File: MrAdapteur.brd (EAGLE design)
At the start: 91 x 41.3 mm, 12 parts, among them J1 PIN2F061.080, J2 PIN2F061.080, X1 1751248

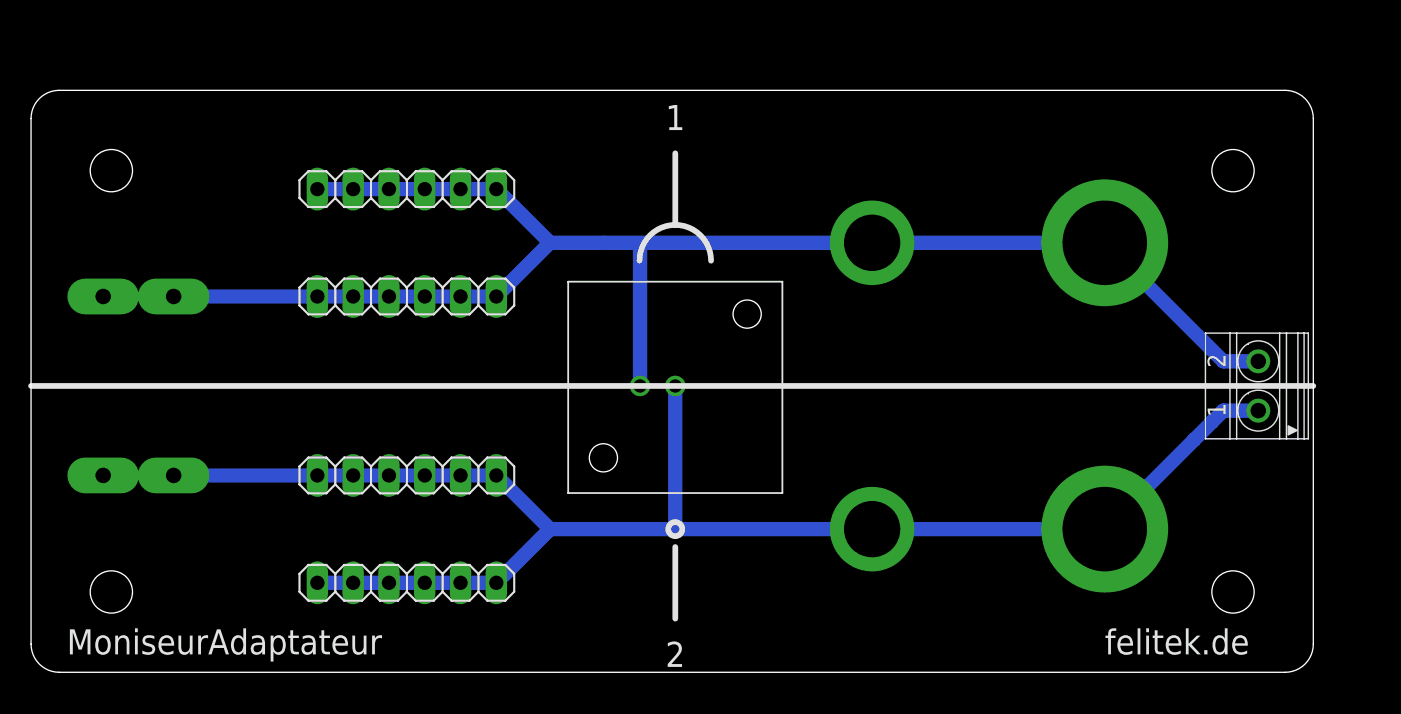
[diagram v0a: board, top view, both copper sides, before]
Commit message: Added standard DC jack, 4.75mm flat connector and wire loop for attaching alligator clips or scope probes
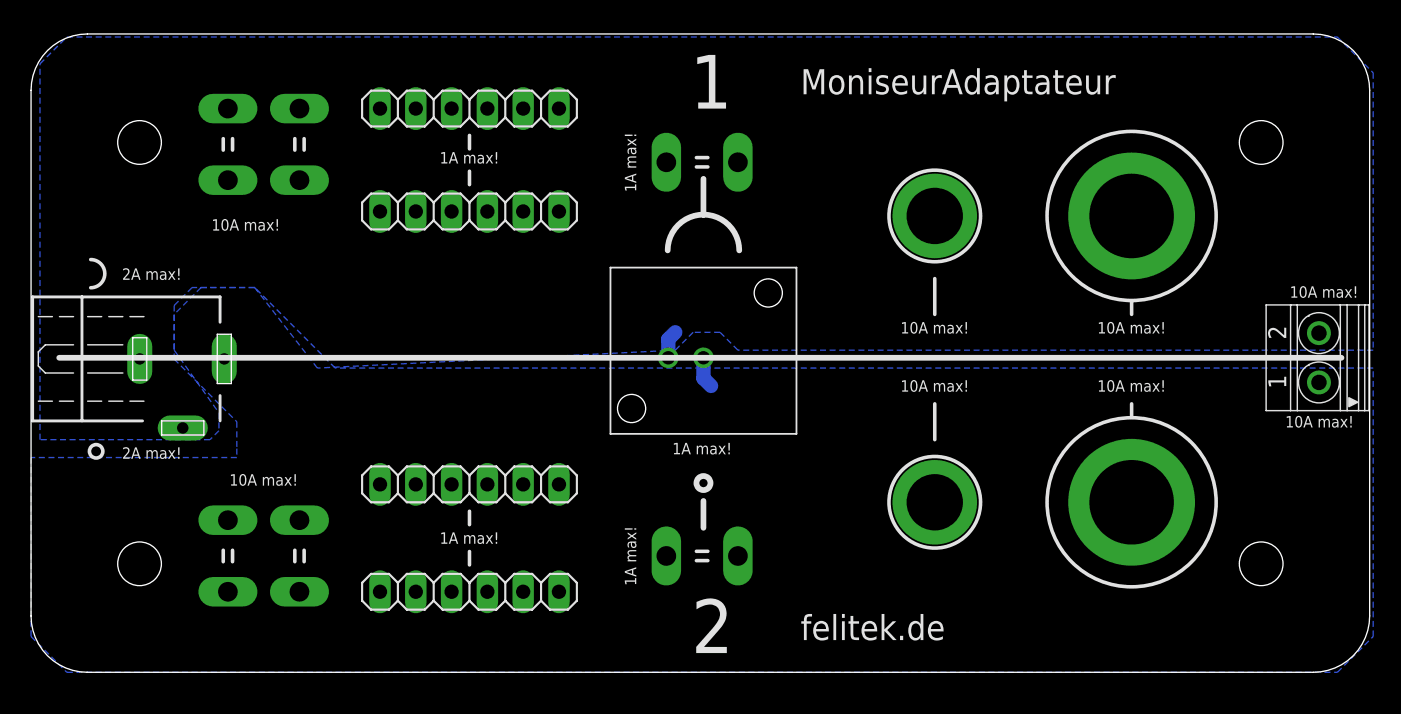
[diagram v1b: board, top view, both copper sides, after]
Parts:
- removed J1, J2: PIN2F061.080, con-faston:F061.080
- added X2: NEB21R, con-lumberg:NEB21R
- added X3, X4, X5, X6, X7, X8: (no value), con-rib:ST4,8
- moved JP2 7.49 mm to (31.1, 32.7)
- moved JP4 7.24 mm to (31.1, 40.0)
- moved U$3 4.84 mm to (64.1, 12.1)
- moved U$4 4.84 mm to (64.1, 32.4)
- moved X1 4.75 mm to (91.3, 22.3)
- moved JP1 4.49 mm to (31.1, 5.71)
- moved JP3 4.49 mm to (31.1, 13.3)
- moved U$5 2.83 mm to (47.7, 22.3)
- moved U$1 2.69 mm to (78.1, 12.1)
- moved U$2 2.69 mm to (78.1, 32.4)
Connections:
- net N$1: now also X2.1, X3.1, X3.2, X5.1, X5.2, X7.1, X7.2; no longer J1.1A, J1.1B
- net N$3: now also X2.2, X2.3, X4.1, X4.2, X6.1, X6.2, X8.1, X8.2; no longer J2.1A, J2.1B
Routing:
- net N$3: track 112.8 -> 2.02 mm
- net N$1: track 110.3 -> 2.22 mm
- added copper zone on layer 16, net N$1
- added copper zone on layer 16, net N$3
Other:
- board size 91 x 41.3 mm -> 95 x 45.3 mm
- board text added: "10A max!"
- board text added: "1A max!"
- board text added: "2A max!"
